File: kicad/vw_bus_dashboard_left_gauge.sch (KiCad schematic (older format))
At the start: 26 parts, among them J1 Conn_01x04, J2 Conn_01x01, J3 Conn_01x01, J4 Conn_01x01, J5 Conn_01x01, U1 TLC59116-Q1

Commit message: Adding DigiKey product numbers
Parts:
- C1: DigiKey (none) -> 478-6048-1-ND
- D1: DigiKey 1080-1597-1-ND -> 516-3974-1-ND
- D2: DigiKey 1080-1597-1-ND -> 754-1890-ND
- D5: DigiKey 754-1890-ND -> 1080-1597-1-ND
- D6: DigiKey 516-3974-1-ND -> 1080-1597-1-ND
- J1: DigiKey (none) -> 455-1804-1-ND
- R1: value R_US -> 750; DigiKey (none) -> 311-750ARCT-ND
- R2, R3, R4: value R_US -> 10k; DigiKey (none) -> 311-10.0KCRCT-ND
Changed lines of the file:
@@
 F 2 "LED_THT:LED_D5.0mm" H 5650 2050 50  0001 C CNN
 F 3 "~" H 5650 2050 50  0001 C CNN
-F 4 "1080-1597-1-ND" V 5650 2050 50  0001 C CNN "DigiKey"
+F 4 "516-3974-1-ND" V 5500 1550 50  0001 C CNN "DigiKey"
 	1    5650 2050
 	0    -1   -1   0
@@
 F 2 "LED_THT:LED_D5.0mm" H 6250 2050 50  0001 C CNN
 F 3 "~" H 6250 2050 50  0001 C CNN
-F 4 "1080-1597-1-ND" V 6250 2050 50  0001 C CNN "DigiKey"
+F 4 "754-1890-ND" V 6250 2050 50  0001 C CNN "DigiKey"
 	1    6250 2050
 	0    -1   -1   0
@@
 F 2 "LED_THT:LED_D5.0mm" H 8050 2050 50  0001 C CNN
 F 3 "~" H 8050 2050 50  0001 C CNN
-F 4 "754-1890-ND" V 8050 2050 50  0001 C CNN "DigiKey"
+F 4 "1080-1597-1-ND" V 8050 2050 50  0001 C CNN "DigiKey"
 	1    8050 2050
 	0    -1   -1   0
@@
 F 2 "LED_THT:LED_D5.0mm" H 8750 2050 50  0001 C CNN
 F 3 "~" H 8750 2050 50  0001 C CNN
-F 4 "516-3974-1-ND" V 8750 2050 50  0001 C CNN "DigiKey"
+F 4 "1080-1597-1-ND" V 8750 2050 50  0001 C CNN "DigiKey"
 	1    8750 2050
 	0    -1   -1   0
@@
 F 2 "Connector_JST:JST_SH_SM04B-SRSS-TB_1x04-1MP_P1.00mm_Horizontal" H 4850 4750 50  0001 C CNN
 F 3 "~" H 4850 4750 50  0001 C CNN
+F 4 "455-1804-1-ND" H 4850 4750 50  0001 C CNN "DigiKey"
 	1    4850 4750
 	-1   0    0    -1
@@
 P 3850 3850
 F 0 "R1" H 3918 3896 50  0000 L CNN
-F 1 "R_US" H 3918 3805 50  0000 L CNN
+F 1 "750" H 3918 3805 50  0000 L CNN
 F 2 "Resistor_SMD:R_0805_2012Metric_Pad1.15x1.40mm_HandSolder" V 3890 3840 50  0001 C CNN
 F 3 "~" H 3850 3850 50  0001 C CNN
+F 4 "311-750ARCT-ND" H 3850 3850 50  0001 C CNN "DigiKey"
 	1    3850 3850
 	1    0    0    -1
@@
 P 3900 3350
 F 0 "R4" V 3800 3400 50  0000 L CNN
-F 1 "R_US" V 3800 3150 50  0000 L CNN
+F 1 "10k" V 3800 3150 50  0000 L CNN
 F 2 "Resistor_SMD:R_0805_2012Metric_Pad1.15x1.40mm_HandSolder" V 3940 3340 50  0001 C CNN
 F 3 "~" H 3900 3350 50  0001 C CNN
+F 4 "311-10.0KCRCT-ND" H 3900 3350 50  0001 C CNN "DigiKey"
 	1    3900 3350
 	0    -1   -1   0
@@
 F 2 "Capacitor_SMD:C_0805_2012Metric_Pad1.15x1.40mm_HandSolder" H 3538 1800 50  0001 C CNN
 F 3 "~" H 3500 1950 50  0001 C CNN
+F 4 "478-6048-1-ND" H 3500 1950 50  0001 C CNN "DigiKey"
 	1    3500 1950
 	1    0    0    -1
@@
 P 3100 2100
 F 0 "R3" H 3168 2146 50  0000 L CNN
-F 1 "R_US" H 3168 2055 50  0000 L CNN
+F 1 "10k" H 3168 2055 50  0000 L CNN
 F 2 "Resistor_SMD:R_0805_2012Metric_Pad1.15x1.40mm_HandSolder" V 3140 2090 50  0001 C CNN
 F 3 "~" H 3100 2100 50  0001 C CNN
+F 4 "311-10.0KCRCT-ND" H 3100 2100 50  0001 C CNN "DigiKey"
 	1    3100 2100
 	1    0    0    -1
@@
 P 2750 2100
 F 0 "R2" H 2818 2146 50  0000 L CNN
-F 1 "R_US" H 2818 2055 50  0000 L CNN
+F 1 "10k" H 2818 2055 50  0000 L CNN
 F 2 "Resistor_SMD:R_0805_2012Metric_Pad1.15x1.40mm_HandSolder" V 2790 2090 50  0001 C CNN
 F 3 "~" H 2750 2100 50  0001 C CNN
+F 4 "311-10.0KCRCT-ND" H 2750 2100 50  0001 C CNN "DigiKey"
 	1    2750 2100
 	1    0    0    -1

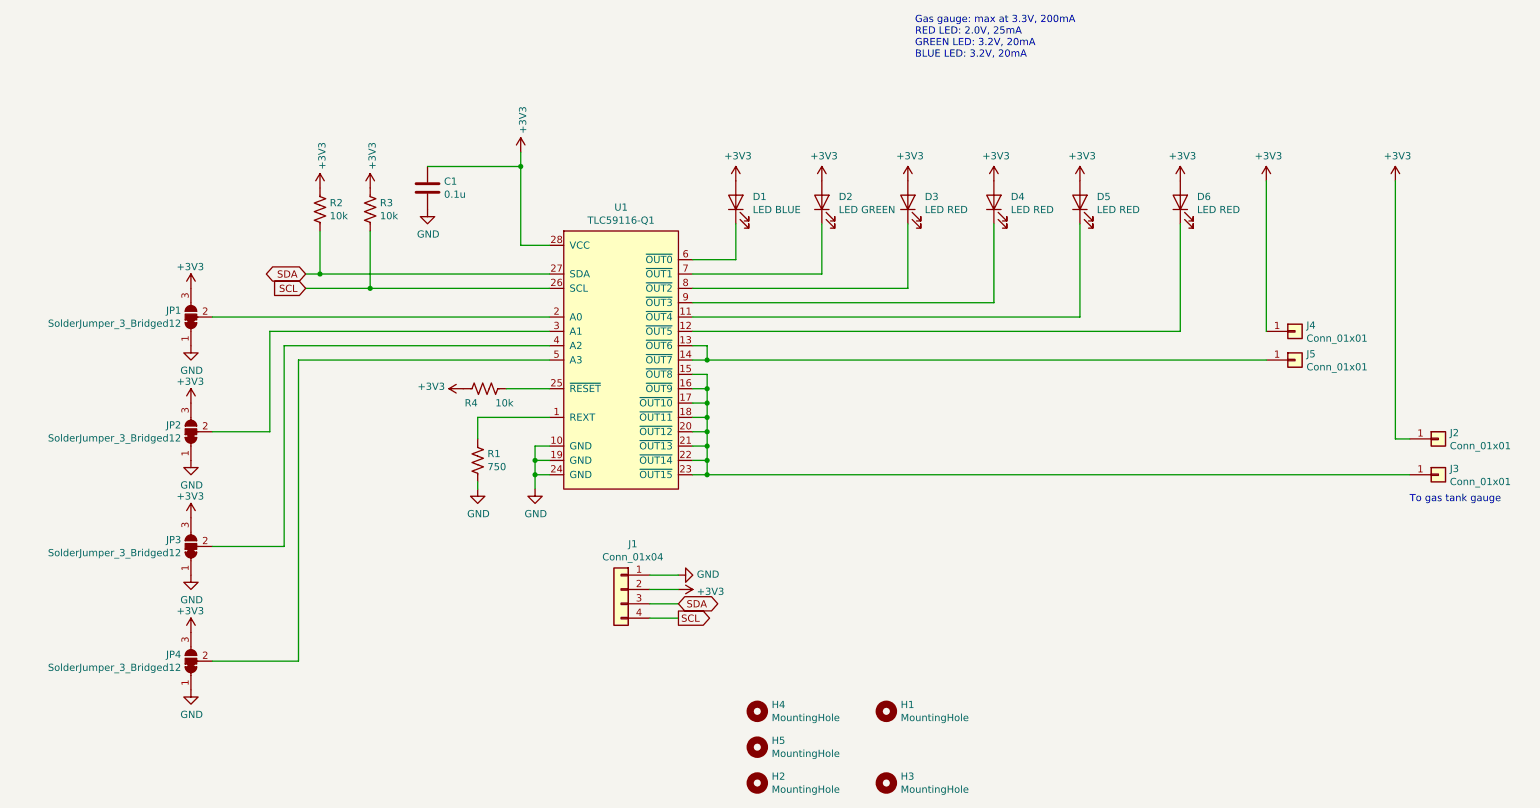
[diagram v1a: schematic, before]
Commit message: Rev 2 using NeoPixels
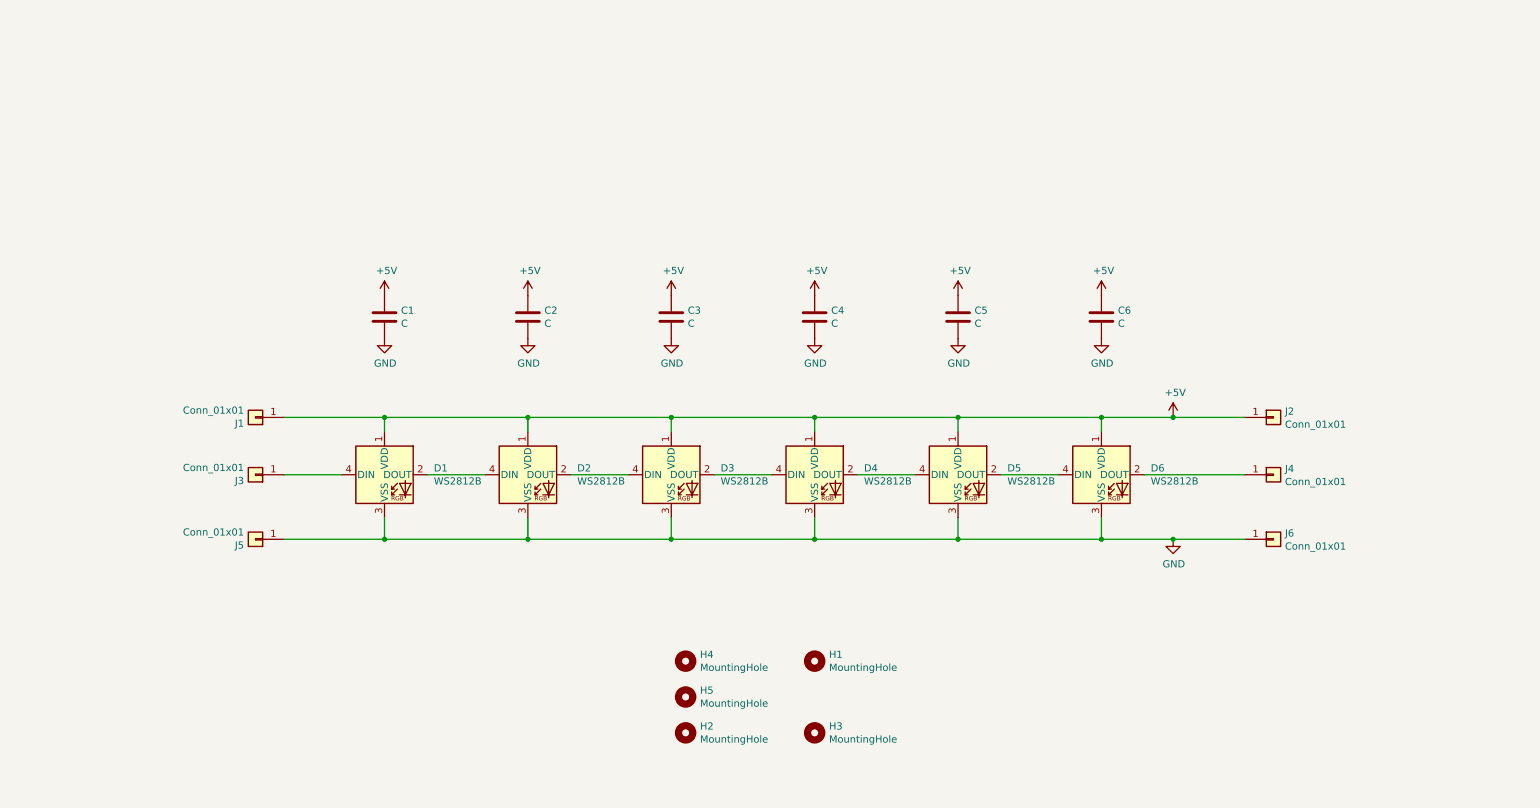
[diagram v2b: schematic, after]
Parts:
- removed D1: LED BLUE, LED_THT:LED_D5.0mm, symbol Device:LED
- removed D2: LED GREEN, LED_THT:LED_D5.0mm, symbol Device:LED
- removed D3, D4, D5, D6: LED RED, LED_THT:LED_D5.0mm, symbol Device:LED
- removed J1: Conn_01x04, Connector_JST:JST_SH_SM04B-SRSS-TB_1x04-1MP_P1.00mm_Horizontal, symbol Connector_Generic:Conn_01x04
- removed JP1, JP2, JP3, JP4: SolderJumper_3_Bridged12, Jumper:SolderJumper-3_P1.3mm_Bridged12_RoundedPad1.0x1.5mm_NumberLabels, symbol Jumper:SolderJumper_3_Bridged12
- removed R1: 750, Resistor_SMD:R_0805_2012Metric_Pad1.15x1.40mm_HandSolder, symbol Device:R_US
- removed R2, R3, R4: 10k, Resistor_SMD:R_0805_2012Metric_Pad1.15x1.40mm_HandSolder, symbol Device:R_US
- removed U1: TLC59116-Q1, Package_SO:TSSOP-28_4.4x9.7mm_P0.65mm, symbol Driver_LED:TLC59116-Q1
- added C2, C3, C4, C5, C6: C, Capacitor_SMD:C_0603_1608Metric, symbol Device:C
- added D1, D2, D3, D4, D5, D6: WS2812B, LED_SMD:LED_WS2812B_PLCC4_5.0x5.0mm_P3.2mm, symbol LED:WS2812B
- added J4, J6: Conn_01x01, Connector_Wire:SolderWirePad_1x01_SMD_5x10mm, symbol Connector_Generic:Conn_01x01
- C1: value 0.1u -> C; footprint Capacitor_SMD:C_0805_2012Metric_Pad1.15x1.40mm_HandSolder -> Capacitor_SMD:C_0603_1608Metric; DigiKey 478-6048-1-ND -> (none)
- J1: renamed from J4; footprint TestPoint:TestPoint_Pad_4.0x4.0mm -> Connector_Wire:SolderWirePad_1x01_SMD_5x10mm
- J2, J3, J5: footprint TestPoint:TestPoint_Pad_4.0x4.0mm -> Connector_Wire:SolderWirePad_1x01_SMD_5x10mm
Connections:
- net GND: now also J5.1 (Pin_1), C2.2, C3.2, C4.2, C5.2, C6.2, D1.3 (VSS), D2.3 (VSS), D3.3 (VSS), D4.3 (VSS), D5.3 (VSS), D6.3 (VSS), J6.1 (Pin_1)
- net at J3.1 (Pin_1): now also D1.4 (DIN)
- net +3V3 renamed +5V
- net +5V: now also C2.1, C3.1, C4.1, C5.1, C6.1, D1.1 (VDD), D2.1 (VDD), D3.1 (VDD), D4.1 (VDD), D5.1 (VDD), D6.1 (VDD)
- new net: D1.2 (DOUT), D2.4 (DIN)
- new net: D2.2 (DOUT), D3.4 (DIN)
- new net: D3.2 (DOUT), D4.4 (DIN)
- new net: D4.2 (DOUT), D5.4 (DIN)
- new net: D5.2 (DOUT), D6.4 (DIN)
- new net: D6.2 (DOUT), J4.1 (Pin_1)
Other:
- note removed: "Gas gauge: max at 3.3V, 200mA\nRED LED: 2.0V, 25mA\nGREEN LED: 3.2V, 20mA\nBLUE LED: 3.2V, 20mA\n"
- note removed: "To gas tank gauge"
- moved on the sheet: H1, H2, H3, H4, H5, J1
